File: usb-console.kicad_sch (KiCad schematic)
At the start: 0 parts

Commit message: [#1] WIP: Change components to ones from the global library, refactor schematic
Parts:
- added C2, C5, C7: C-100n-0402, DW-footprints:C_0402_1005Metric, symbol DW-capacitors:C-100n-0402
- added D3, D6: LED-R-0603_KT-0603R, DW-footprints:LED_0603_1608Metric_R, symbol DW-diodes:LED-R-0603_KT-0603R
- added D5: PUSB3F96X, DW-footprints:SOT1176-1, symbol DW-TVS:PUSB3F96X
- added J4: USB-C_USB-310F-B-SU, DW-footprints:USB-C-Receptacle_USB-310F-B-SU, symbol DW-connectors:USB-C_USB-310F-B-SU
- added R21, R6: R-5k1-0402, DW-footprints:R_0402_1005Metric, symbol DW-resistors:R-5k1-0402
- added R5: R-330r-0402, DW-footprints:R_0402_1005Metric, symbol DW-resistors:R-330r-0402
- added R7, R8: R-1k-0402, DW-footprints:R_0402_1005Metric, symbol DW-resistors:R-1k-0402
- added U2: FT230XQ-R, DW-footprints:QFN-16-1EP_4x4mm_P0.65mm_EP2.15x2.15mm, symbol DW-ICs:FT230XQ-R
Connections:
- new net: D3.2 (A), R8.1
- new net: D6.2 (A), R7.1
- new net: C2.2, J4.S1 (SHIELD), R5.2
- new net +VBUS: C5.2, J4.A4 (VBUS), J4.A9 (VBUS), J4.B4 (VBUS), J4.B9 (VBUS), U2.10 (V_{CC})
- new net CC1: D5.5 (CH4), D5.6 (CH4), J4.A5 (CC1), R6.2
- new net CC2: D5.4 (CH3), D5.7 (CH3), J4.B5 (CC2), R21.2
- new net FTDI_CBUS0: U2.12 (CBUS0)
- new net FTDI_CBUS3: U2.14 (CBUS3)
- new net FTDI_LED_RX: D3.1 (C), U2.11 (CBUS1)
- new net FTDI_LED_TX: D6.1 (C), U2.5 (CBUS2)
- new net FTDI_RX: U2.2 (RXD)
- new net FTDI_TX: U2.15 (TXD)
- new net FTDI_VCCIO: C7.2, R7.2, R8.2, U2.1 (V_{CCIO}), U2.8 (3V3_{OUT})
- new net GND: C2.1, C5.1, C7.1, D5.3 (GND), D5.8 (GND), J4.A1 (GND), J4.A12 (GND), J4.B1 (GND), J4.B12 (GND), R21.1, R5.1, R6.1, U2.13 (GND), U2.17 (GND), U2.3 (GND)
- new net USB_D+: D5.2 (CH2), D5.9 (CH2), J4.A6 (D+), J4.B6 (D+), U2.6 (D+)
- new net USB_D-: D5.1 (CH1), D5.10 (CH1), J4.A7 (D-), J4.B7 (D-), U2.7 (D-)
- no-connect marks 0 -> 4
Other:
- note added: "USB-C console"

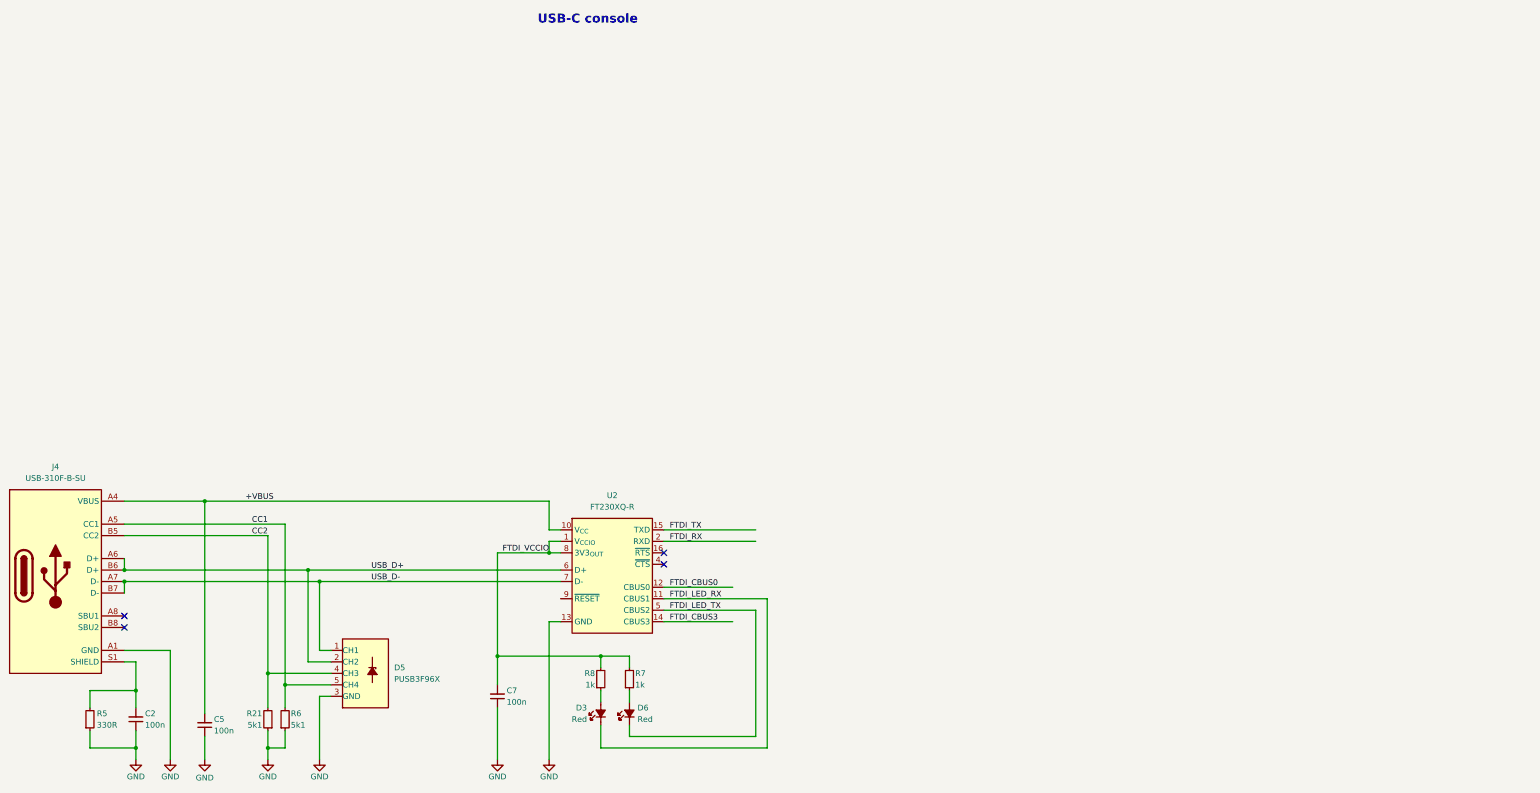
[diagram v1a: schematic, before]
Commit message: [#1] Change components to ones from the global library, add debug console, refactor schematic
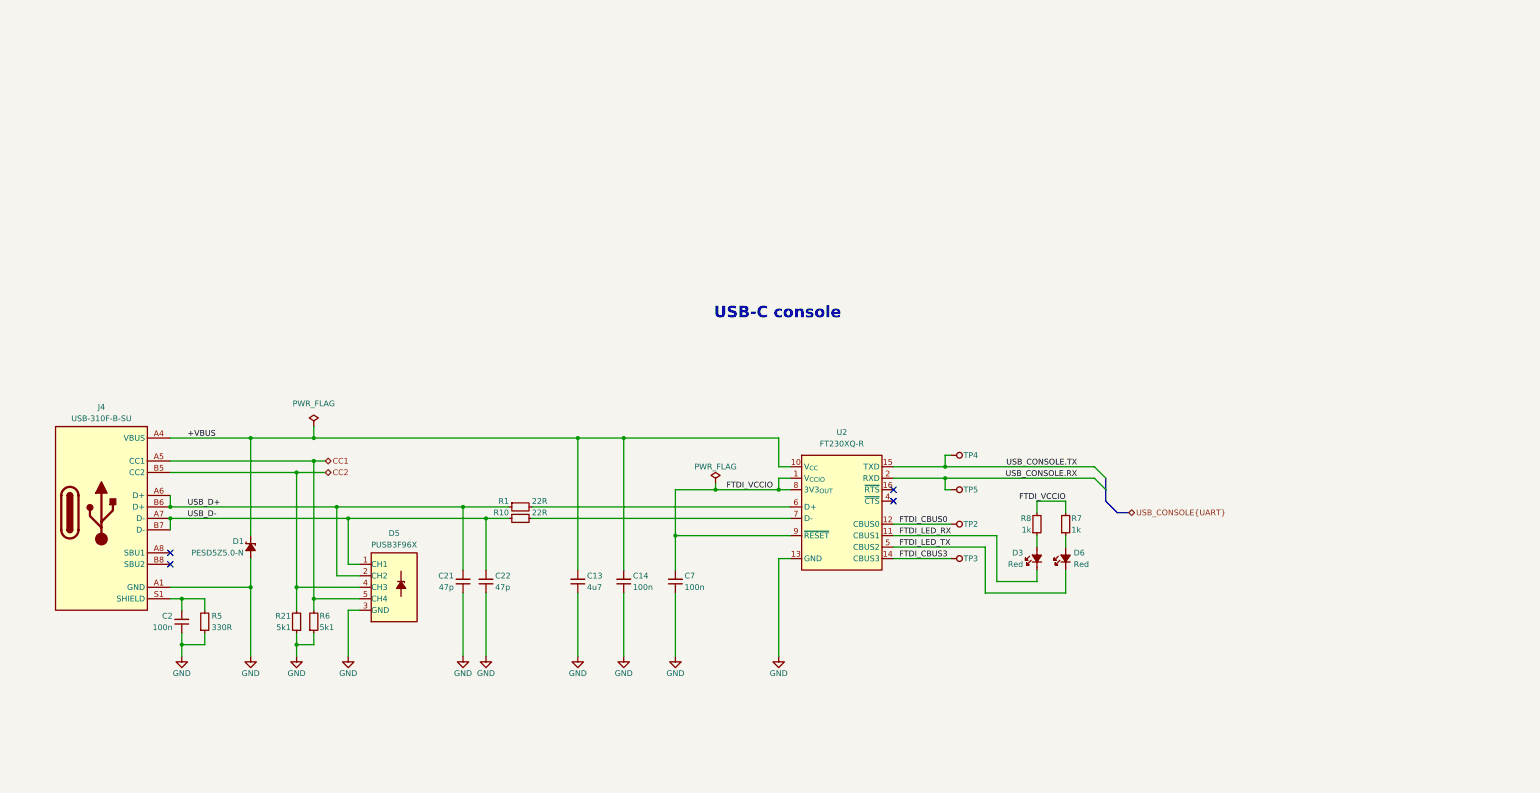
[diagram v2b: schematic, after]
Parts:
- removed C5: C-100n-0402, DW-footprints:C_0402_1005Metric, symbol DW-capacitors:C-100n-0402
- added C13: C-4u7-0402, DW-footprints:C_0402_1005Metric, symbol DW-capacitors:C-4u7-0402
- added C14: C-100n-0402, DW-footprints:C_0402_1005Metric, symbol DW-capacitors:C-100n-0402
- added C21, C22: C-47p-0402, DW-footprints:C_0402_1005Metric, symbol DW-capacitors:C-47p-0402
- added D1: PESD5Z5, DW-footprints:D_SOD-523, symbol DW-TVS:PESD5Z5
- added R1, R10: R-22R-0402, DW-footprints:R_0402_1005Metric, symbol DW-resistors:R-22R-0402
- added TP2, TP3, TP4, TP5: TP_SMD_0.75mm, DW-footprints:TP_SMD_0.75mm, symbol DW-test-points:TP_SMD_0.75mm
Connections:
- net +VBUS: now also C13.2, C14.2, D1.1 (C)
- net FTDI_CBUS0: now also TP2.1
- net FTDI_CBUS3: now also TP3.1
- net FTDI_VCCIO: now also U2.9 (~{RESET})
- net GND: now also C13.1, C14.1, C21.1, C22.1, D1.2 (A)
- net USB_D+: now also C21.2, R1.1; no longer U2.6 (D+)
- net USB_D-: now also C22.2, R10.1; no longer U2.7 (D-)
- net FTDI_RX renamed USB_CONSOLE.RX
- net USB_CONSOLE.RX: now also TP5.1
- net FTDI_TX renamed USB_CONSOLE.TX
- net USB_CONSOLE.TX: now also TP4.1
- new net: R1.2, U2.6 (D+)
- new net: R10.2, U2.7 (D-)
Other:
- moved on the sheet: C2, C7, D3, D5, D6, J4, R21, R5, R6, R7, R8, U2

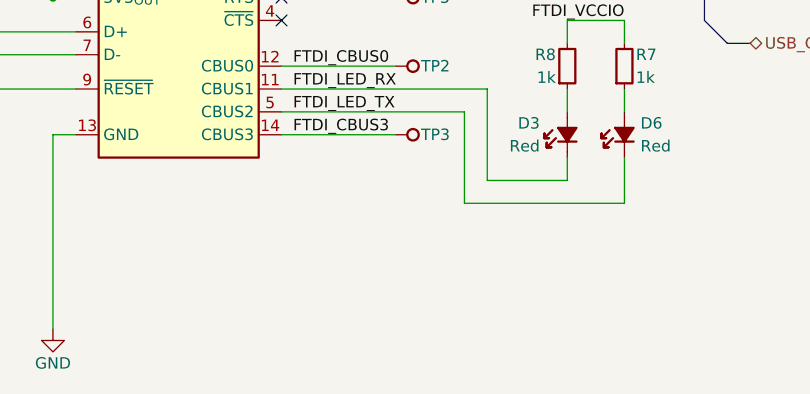
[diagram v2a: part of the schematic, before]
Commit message: [#1] Add debug UART connector
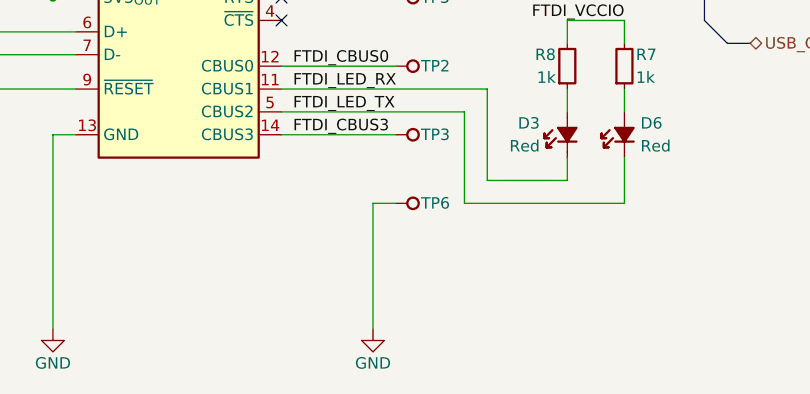
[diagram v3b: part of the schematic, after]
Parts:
- added TP6: TP_SMD_0.75mm, DW-footprints:TP_SMD_0.75mm, symbol DW-test-points:TP_SMD_0.75mm
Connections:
- net GND: now also TP6.1
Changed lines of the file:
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@@
+	(wire
+		(pts
+			(xy 261.62 161.29) (xy 264.16 161.29)
+		)
+		(stroke
+			(width 0)
+			(type default)
+		)
+	)
 	(wire
 		(pts
@@
 		(pts
 			(xy 264.16 138.43) (xy 262.89 138.43)
+		)
+		(stroke
+			(width 0)
+			(type default)
+		)
+	)
+	(wire
+		(pts
+			(xy 261.62 161.29) (xy 261.62 175.26)
 		)
 		(stroke
@@
 				(path "/090a8e41-87a8-4fb1-998b-60a2c0dc4cee/05afd91b-987f-4955-bfc3-ea0accf4f845"
 					(reference "C13")
+					(unit 1)
+				)
+			)
+		)
+	)
+	(symbol
+		(lib_id "DW-test-points:TP_SMD_0.75mm")
+		(at 264.16 161.29 0)
+		(unit 1)
+		(exclude_from_sim no)
+		(in_bom no)
+		(on_board yes)
+		(dnp no)
+		(property "Reference" "TP6"
+			(at 266.954 161.29 0)
+			(effects
+				(font
+					(size 1.27 1.27)
+					(thickness 0.15)
+				)
+				(justify left)
+			)
+		)
+		(property "Value" "TP_SMD_0.75mm"
+			(at 267.97 163.83 0)
+			(effects
+				(font
+					(size 1.27 1.27)
+					(thickness 0.15)
+				)
+				(justify left bottom)
+				(hide yes)
+			)
+		)
+		(property "Footprint" "DW-footprints:TP_SMD_0.75mm"
+			(at 267.97 166.37 0)
+			(effects
+				(font
+					(size 1.27 1.27)
+					(thickness 0.15)
+				)
+				(justify left bottom)
+				(hide yes)
+			)
+		)
+		(property "Datasheet" ""
+			(at 267.97 168.91 0)
+			(effects
+				(font
+					(size 1.27 1.27)
+					(thickness 0.15)
+				)
+				(justify left bottom)
+				(hide yes)
+			)
+		)
+		(property "Description" "Test point, SMD, round, 0.75mm diameter"
+			(at 267.97 171.45 0)
+			(effects
+				(font
+					(size 1.27 1.27)
+					(thickness 0.15)
+				)
+				(justify left bottom)
+				(hide yes)
+			)
+		)
+		(pin "1"
+		)
+		(instances
+			(project "cm5-module"
+				(path "/090a8e41-87a8-4fb1-998b-60a2c0dc4cee/05afd91b-987f-4955-bfc3-ea0accf4f845"
+					(reference "TP6")
 					(unit 1)
 				)
@@
 					(unit 1)
 				)
+			)
+		)
+	)
+	(symbol
+		(lib_id "DW-power-symbols:GND")
+		(at 261.62 175.26 0)
+		(mirror y)
+		(unit 1)
+		(exclude_from_sim no)
+		(in_bom yes)
+		(on_board yes)
+		(dnp no)
+		(property "Reference" "#PWR0416"
+			(at 261.62 181.61 0)
+			(effects
+				(font
+					(size 1.27 1.27)
+				)
+				(hide yes)
+			)
+		)
+		(property "Value" "GND"
+			(at 261.62 179.07 0)
+			(effects
+				(font
+					(size 1.27 1.27)
+				)
+			)
+		)
+		(property "Footprint" ""
+			(at 261.62 175.26 0)
+			(effects
+				(font
+					(size 1.27 1.27)
+				)
+				(hide yes)
+			)
+		)
+		(property "Datasheet" ""
+			(at 261.62 175.26 0)
+			(effects
+				(font
+					(size 1.27 1.27)
+				)
+				(hide yes)
+			)
+		)
+		(property "Description" "Power symbol creates a global label with name \"GND\" , ground"
+			(at 261.62 175.26 0)
+			(effects
+				(font
+					(size 1.27 1.27)
+				)
+				(hide yes)
+			)
+		)
+		(pin "1"
+		)
+		(instances
+			(project "cm5-module"
+				(path "/090a8e41-87a8-4fb1-998b-60a2c0dc4cee/05afd91b-987f-4955-bfc3-ea0accf4f845"
+					(reference "#PWR0416")
+					(unit 1)
+				)

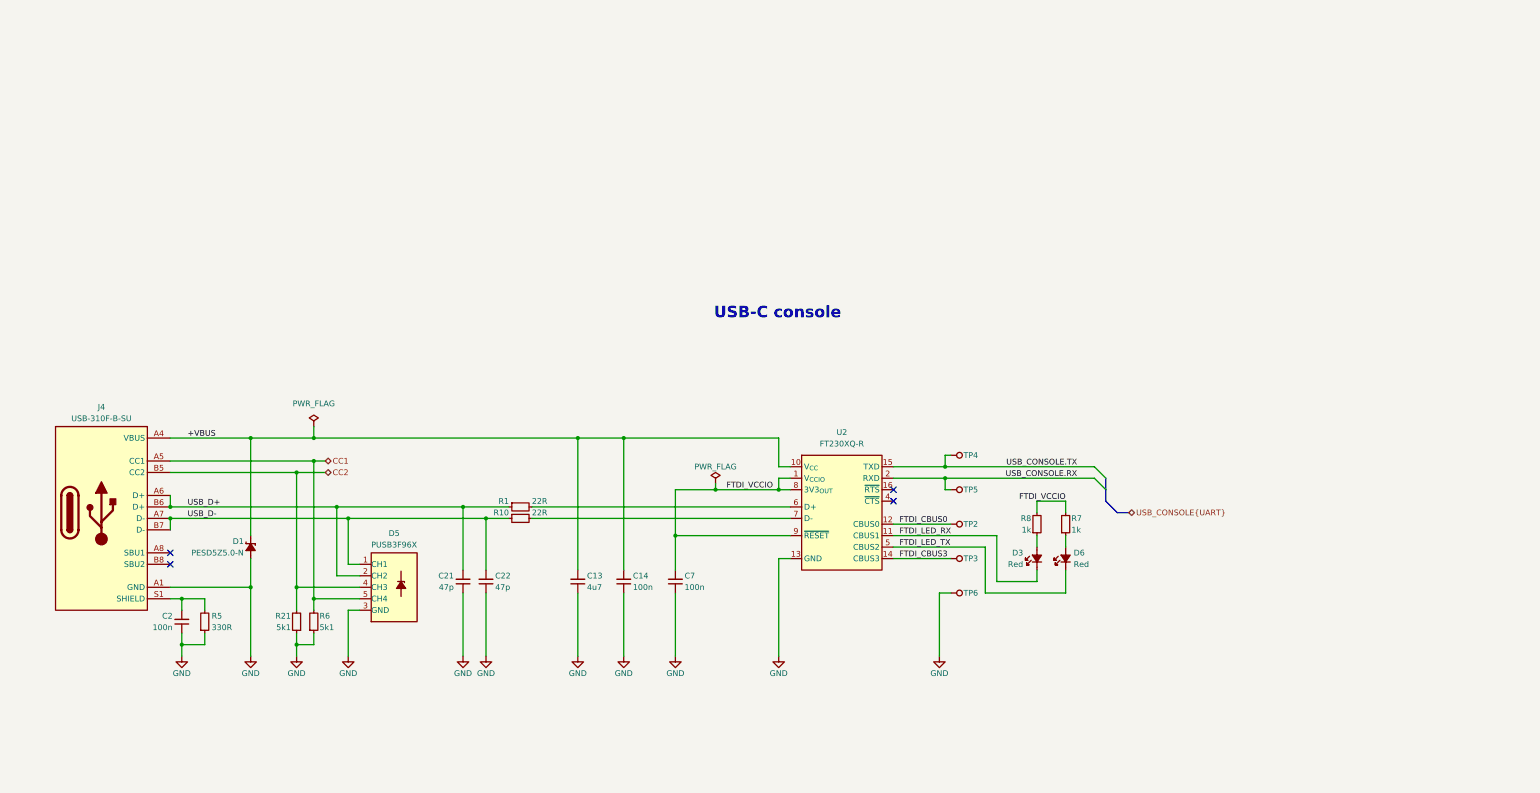
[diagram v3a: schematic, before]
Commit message: [#1] Add level shifter for UART debug, update footprints from library
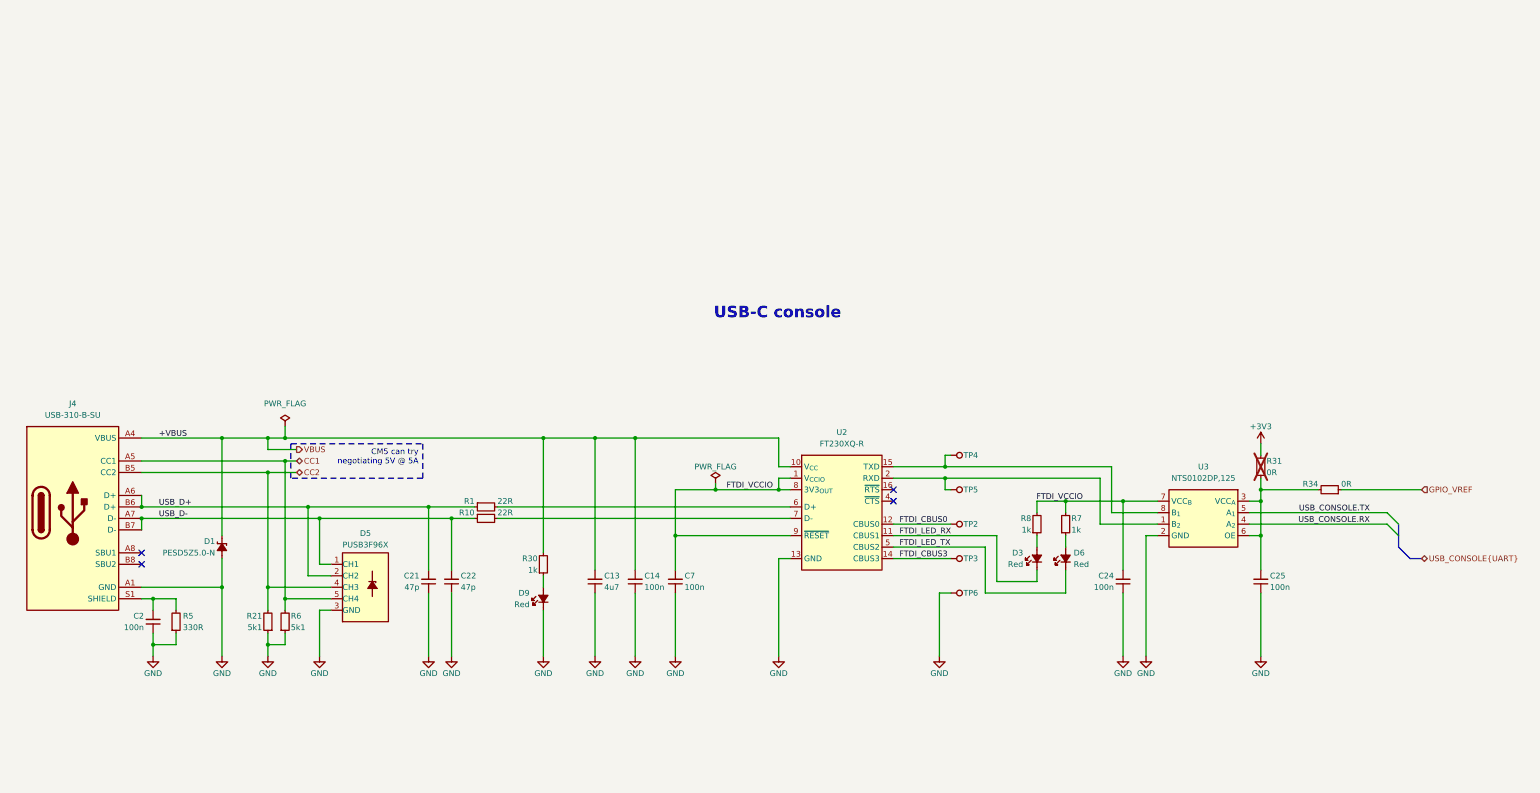
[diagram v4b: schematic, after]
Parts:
- added C24, C25: C-100n-0402, DW-footprints:C_0402_1005Metric, symbol DW-capacitors:C-100n-0402
- added D9: LED-R-0603_KT-0603R, DW-footprints:LED_0603_1608Metric_R, symbol DW-diodes:LED-R-0603_KT-0603R
- added R30: R-1k-0402, DW-footprints:R_0402_1005Metric, symbol DW-resistors:R-1k-0402
- added R31, R34: R-0R-0402, DW-footprints:R_0402_1005Metric, symbol DW-resistors:R-0R-0402
- added U3: NTS0102DP, DW-footprints:TSSOP-8_3x3mm_P0.65mm, symbol DW-ICs:NTS0102DP
- J4: footprint DW-footprints:USB-C-Receptacle_USB-310F-B-SU -> DW-footprints:USB-C-Receptacle_USB-310-B-SU; symbol DW-connectors:USB-C_USB-310F-B-SU -> DW-connectors:USB-C_USB-310-B-SU; LCSC C309365 -> C309347; MPN USB-310F-B-SU -> USB-310-B-SU
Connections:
- net FTDI_VCCIO: now also C24.2, U3.7 (VCC_{B})
- net GND: now also C24.1, C25.1, D9.1 (C), U3.2 (GND)
- net USB_CONSOLE.RX: now also U3.4 (A_{2}); no longer TP5.1, U2.2 (RXD)
- net USB_CONSOLE.TX: now also U3.5 (A_{1}); no longer TP4.1, U2.15 (TXD)
- net +VBUS renamed VBUS
- net VBUS: now also R30.2
- new net: D9.2 (A), R30.1
- new net: TP5.1, U2.2 (RXD), U3.1 (B_{2})
- new net: C25.2, R31.2, R34.2, U3.3 (VCC_{A}), U3.6 (OE)
- new net: TP4.1, U2.15 (TXD), U3.8 (B_{1})
- new net +3V3: R31.1
- new net GPIO_VREF: R34.1
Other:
- moved on the sheet: C13, C14, C2, C21, C22, D1, D5, J4, R1, R10, R21, R5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

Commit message: [#1] Re-annotate schematic
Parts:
- renumbered C21 to C13, C22 to C14, C13 to C15, C14 to C16, C7 to C17, C24 to C18, C25 to C19, C2 to C20, D1 to D3, D5 to D4, D3 to D5, D9 to D7, J4 to J9, R31 to R16, R34 to R17, R1 to R18, R10 to R19, R8 to R20, R7 to R21, R30 to R22, R5 to R23, R21 to R24, R6 to R25, TP4 to TP2, TP5 to TP3, TP2 to TP4, TP3 to TP5, U2 to U3, U3 to U4
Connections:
- net CC2: now also D4.1 (CH1), D4.10 (CH1); no longer D4.4 (CH3), D4.7 (CH3)
- net USB_D+: now also D4.4 (CH3), D4.7 (CH3); no longer D4.2 (CH2), D4.9 (CH2)
- net USB_D-: now also D4.2 (CH2), D4.9 (CH2); no longer D4.1 (CH1), D4.10 (CH1)
